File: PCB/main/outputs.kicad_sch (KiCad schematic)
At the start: 1 part

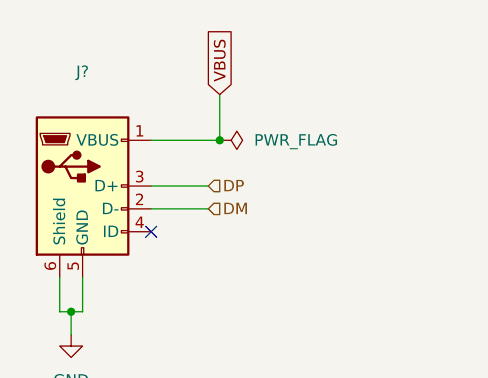
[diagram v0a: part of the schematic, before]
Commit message: updated UVLO circuit
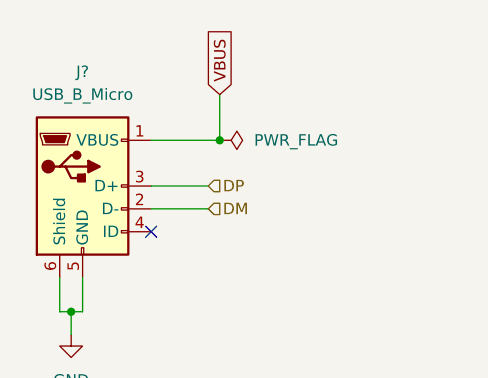
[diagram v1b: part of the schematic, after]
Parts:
- J?: value (none) -> USB_B_Micro
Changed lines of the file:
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@@
     (in_bom yes) (on_board yes) (fields_autoplaced)
     (property "Reference" "J?" (id 0) (at 36.83 20.32 0))
-    (property "Value" "" (id 1) (at 36.83 22.86 0))
+    (property "Value" "USB_B_Micro" (id 1) (at 36.83 22.86 0))
     (property "Footprint" "" (id 2) (at 40.64 34.29 0)
       (effects (font (size 1.27 1.27)) hide)
